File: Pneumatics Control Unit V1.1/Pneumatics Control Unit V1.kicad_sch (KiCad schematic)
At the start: 74 parts, among them J1 TX_PORT, J10 Conn_01x02_Male, J11 Conn_01x02_Male, J12 10118194-0001LF, J2 RX_PORT, J3 MICROMOD-2222, J4 Conn_01x02_Male, J5 Conn_01x02_Male, J6 Conn_01x02_Male, J7 Conn_01x02_Male, J8 Conn_01x02_Male, J9 Conn_01x02_Male, U1 ISL83490IBZ, U2 MIC2178-3.3YWM, U3 MC78M05CDTRKG, U4 MC78M05CDTRKG

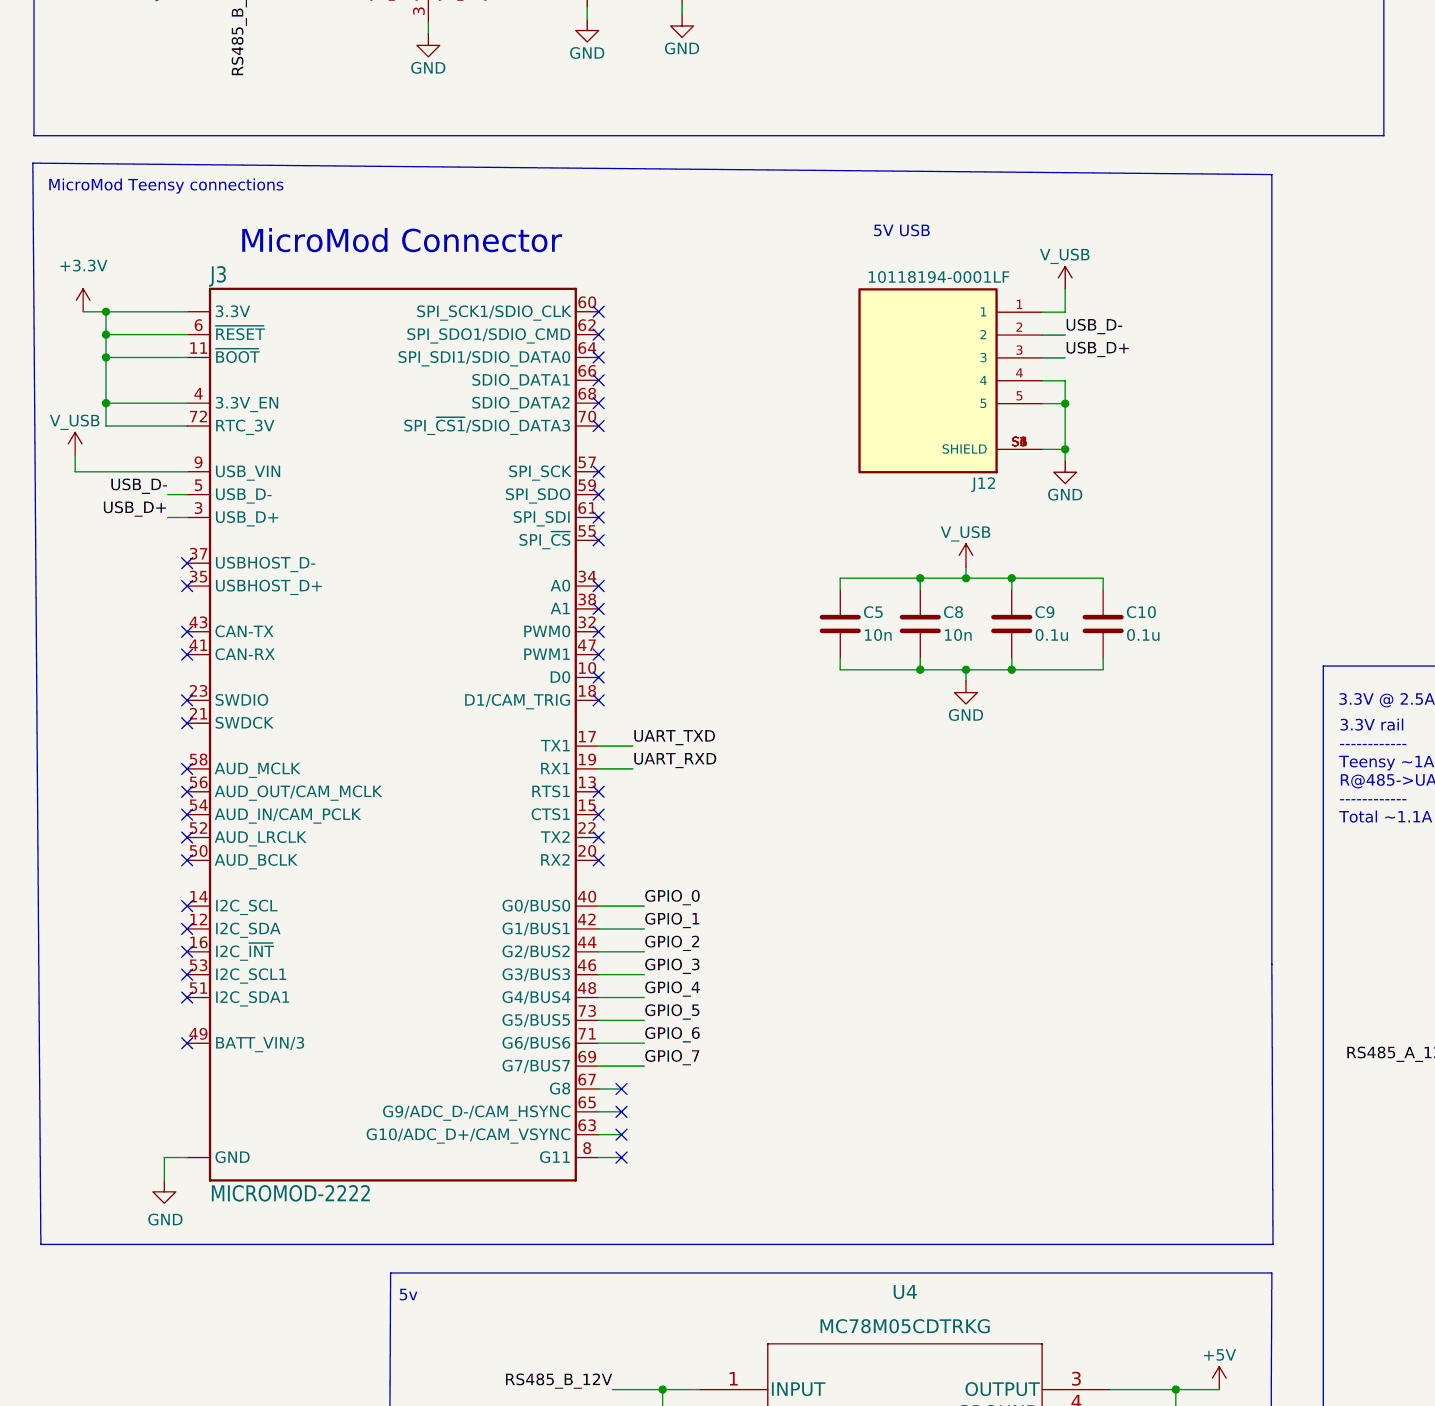
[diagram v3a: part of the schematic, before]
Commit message: Reducing vias, Thicken traces, adding resistors
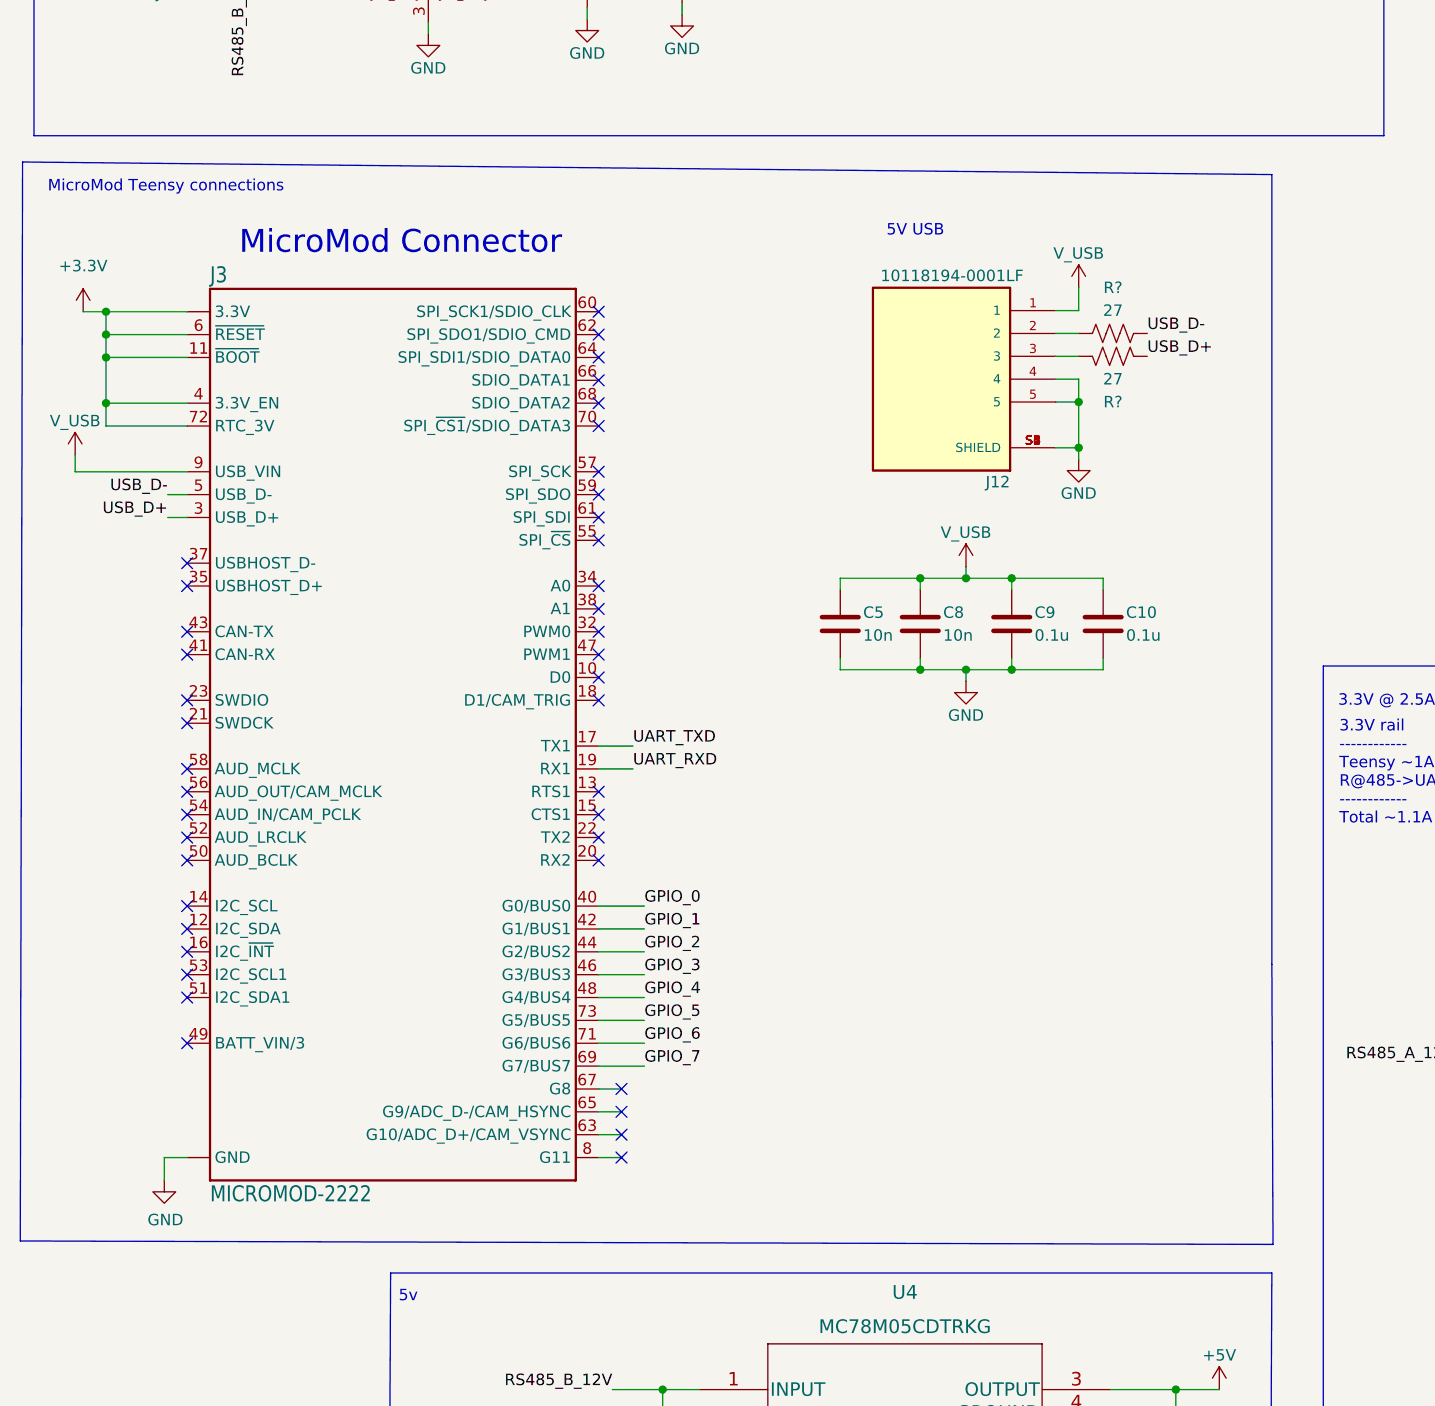
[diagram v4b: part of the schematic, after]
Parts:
- added R? (x2): 27, Resistor_SMD:R_0805_2012Metric_Pad1.20x1.40mm_HandSolder, symbol Device:R_US
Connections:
- net USB_D+: now also R?.2; no longer J12.3
- net USB_D-: now also R?.2; no longer J12.2
- new net: J12.2, R?.1
- new net: J12.3, R?.1
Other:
- moved on the sheet: J12

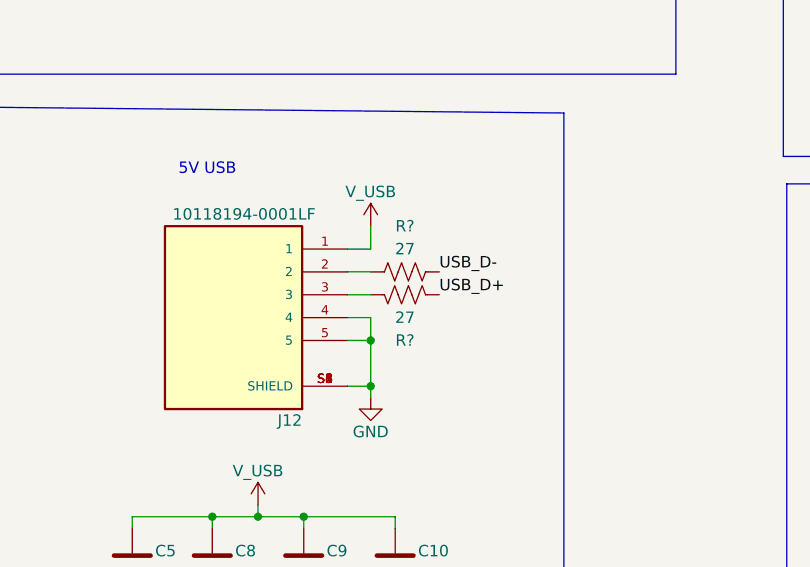
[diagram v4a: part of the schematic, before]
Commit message: Adding more grounding vias, and making the mouting holes 8-32
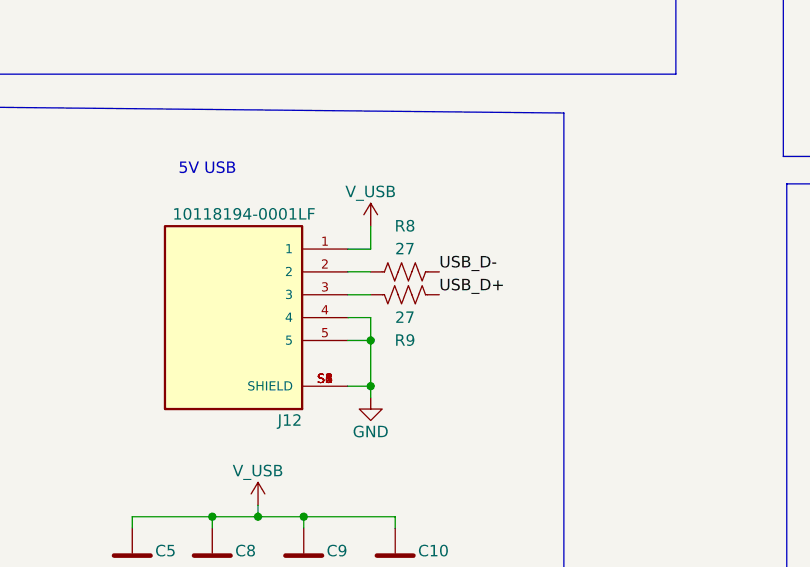
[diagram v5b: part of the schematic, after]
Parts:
- gave numbers to parts that had none: 2
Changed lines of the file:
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@@
   (symbol (lib_id "Device:R_US") (at 135.509 119.761 90) (unit 1)
     (in_bom yes) (on_board yes)
-    (property "Reference" "R?" (id 0) (at 135.509 114.681 90))
+    (property "Reference" "R8" (id 0) (at 135.509 114.681 90))
     (property "Value" "27" (id 1) (at 135.509 117.221 90))
     (property "Footprint" "Resistor_SMD:R_0805_2012Metric_Pad1.20x1.40mm_HandSolder" (id 2) (at 135.763 118.745 90)
@@
   (symbol (lib_id "Device:R_US") (at 135.509 122.301 90) (mirror x) (unit 1)
     (in_bom yes) (on_board yes)
-    (property "Reference" "R?" (id 0) (at 135.509 127.381 90))
+    (property "Reference" "R9" (id 0) (at 135.509 127.381 90))
     (property "Value" "27" (id 1) (at 135.509 124.841 90))
     (property "Footprint" "Resistor_SMD:R_0805_2012Metric_Pad1.20x1.40mm_HandSolder" (id 2) (at 135.763 123.317 90)
@@
     )
     (path "/f09ce1b1-fd65-4ae3-b44f-4ebb4de3bacb"
-      (reference "R?") (unit 1) (value "27") (footprint "Resistor_SMD:R_0805_2012Metric_Pad1.20x1.40mm_HandSolder")
+      (reference "R8") (unit 1) (value "27") (footprint "Resistor_SMD:R_0805_2012Metric_Pad1.20x1.40mm_HandSolder")
     )
     (path "/fcd7e2a1-c75c-4331-9afc-ca74c910ff4d"
-      (reference "R?") (unit 1) (value "27") (footprint "Resistor_SMD:R_0805_2012Metric_Pad1.20x1.40mm_HandSolder")
+      (reference "R9") (unit 1) (value "27") (footprint "Resistor_SMD:R_0805_2012Metric_Pad1.20x1.40mm_HandSolder")
     )
     (path "/097e0edc-0bee-47b5-b180-d68199aa4ff8"

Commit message: Adding 12V capabilities
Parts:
- added U (x2): (no value), symbol Connector:Conn_01x03_Male
- U: renamed from D6; value D_TVS_x2_AAC -> (none); footprint Package_TO_SOT_SMD:SOT-723 -> (none)
- U: renamed from C22; value 1u -> (none); footprint Capacitor_SMD:C_0805_2012Metric_Pad1.18x1.45mm_HandSolder -> (none)
- U: renamed from R7; value 10k -> (none); footprint Resistor_SMD:R_0805_2012Metric_Pad1.20x1.40mm_HandSolder -> (none)
- U: renamed from D10; value D_TVS_x2_AAC -> (none); footprint Package_TO_SOT_SMD:SOT-723 -> (none)
- U: renamed from H1; value MountingHole -> (none); footprint MountingHole:MountingHole_2.5mm -> (none)
- U: renamed from MOSFET5; value SSM3K7002KFU -> (none); footprint SSM3K7002KFU:SSM3K7002KFU -> (none)
- U: renamed from CR1; value MBRS130L -> (none); footprint MBRS130L:MBRS130L -> (none)
- U: renamed from C19; value 22uF -> (none); footprint 22U:CL21A226MQQNNNF -> (none)
- U: renamed from U1; value ISL83490IBZ -> (none); footprint RS_UART:ISL83490IBZ -> (none)
- U: renamed from MOSFET6; value SSM3K7002KFU -> (none); footprint SSM3K7002KFU:SSM3K7002KFU -> (none)
- U: renamed from C9; value 0.1u -> (none); footprint Capacitor_SMD:C_0805_2012Metric_Pad1.18x1.45mm_HandSolder -> (none)
- U: renamed from U4; value MC78M05CDTRKG -> (none); footprint 12v5v:MC78M05CDTRKG -> (none)
- U: renamed from MOSFET8; value SSM3K7002KFU -> (none); footprint SSM3K7002KFU:SSM3K7002KFU -> (none)
- U: renamed from J1; value TX_PORT -> (none); footprint RS485:RS485 -> (none)
- U: renamed from J12; value 10118194-0001LF -> (none); footprint 10118194-0001LF:AMPHENOL_10118194-0001LF -> (none)
- U: renamed from C5; value 10n -> (none); footprint Capacitor_SMD:C_0805_2012Metric_Pad1.18x1.45mm_HandSolder -> (none)
- U: renamed from J8; value Conn_01x02_Male -> (none); footprint Connector_PinSocket_2.54mm:PinSocket_1x02_P2.54mm_Vertical -> (none)
- U: renamed from U3; value MC78M05CDTRKG -> (none); footprint 12v5v:MC78M05CDTRKG -> (none)
- U: renamed from MOSFET3; value SSM3K7002KFU -> (none); footprint SSM3K7002KFU:SSM3K7002KFU -> (none)
- U: renamed from C17; value 22uF -> (none); footprint 22U:CL21A226MQQNNNF -> (none)
- U: renamed from C24; value 1u -> (none); footprint Capacitor_SMD:C_0805_2012Metric_Pad1.18x1.45mm_HandSolder -> (none)
- U: renamed from C18; value 22uF -> (none); footprint 22U:CL21A226MQQNNNF -> (none)
- U: renamed from J6; value Conn_01x02_Male -> (none); footprint Connector_PinSocket_2.54mm:PinSocket_1x02_P2.54mm_Vertical -> (none)
- U: renamed from C11; value CL21A226MQQNNNF (22uF) -> (none); footprint 22U:CL21A226MQQNNNF -> (none)
- U: renamed from C26; value 1u -> (none); footprint Capacitor_SMD:C_0805_2012Metric_Pad1.18x1.45mm_HandSolder -> (none)
- U: renamed from D9; value D_TVS_x2_AAC -> (none); footprint Package_TO_SOT_SMD:SOT-723 -> (none)
- U: renamed from L1; value LB3218T330M (33uH) -> (none); footprint induct33u:LB3218T330M -> (none)
- U: renamed from C6; value 6.8n -> (none); footprint Capacitor_SMD:C_0805_2012Metric_Pad1.18x1.45mm_HandSolder -> (none)
- U: renamed from C12; value 22uF -> (none); footprint 22U:CL21A226MQQNNNF -> (none)
- U: renamed from J9; value Conn_01x02_Male -> (none); footprint Connector_PinSocket_2.54mm:PinSocket_1x02_P2.54mm_Vertical -> (none)
- U: renamed from D1; value D_TVS_x2_AAC -> (none); footprint Package_TO_SOT_SMD:SOT-723 -> (none)
- U: renamed from R6; value 10k -> (none); footprint Resistor_SMD:R_0805_2012Metric_Pad1.20x1.40mm_HandSolder -> (none)
- U: renamed from C10; value 0.1u -> (none); footprint Capacitor_SMD:C_0805_2012Metric_Pad1.18x1.45mm_HandSolder -> (none)
- U: renamed from C15; value 22uF -> (none); footprint 22U:CL21A226MQQNNNF -> (none)
- U: renamed from H3; value MountingHole -> (none); footprint MountingHole:MountingHole_2.5mm -> (none)
- U: renamed from MOSFET2; value SSM3K7002KFU -> (none); footprint SSM3K7002KFU:SSM3K7002KFU -> (none)
- U: renamed from J4; value Conn_01x02_Male -> (none); footprint Connector_PinSocket_2.54mm:PinSocket_1x02_P2.54mm_Vertical -> (none)
- U: renamed from J5; value Conn_01x02_Male -> (none); footprint Connector_PinSocket_2.54mm:PinSocket_1x02_P2.54mm_Vertical -> (none)
- U: renamed from D2; value D_TVS_x2_AAC -> (none); footprint Package_TO_SOT_SMD:SOT-723 -> (none)
- U: renamed from J3; value MICROMOD-2222 -> (none); footprint mm-m:M.2-CONNECTOR-E -> (none)
- U: renamed from D3; value D_TVS_x2_AAC -> (none); footprint Package_TO_SOT_SMD:SOT-723 -> (none)
- U: renamed from U2; value MIC2178-3.3YWM -> (none); footprint 33sw:MIC2178-3.3YWM -> (none)
- U: renamed from C21; value 22uF -> (none); footprint 22U:CL21A226MQQNNNF -> (none)
- U: renamed from R2; value 10 -> (none); footprint Resistor_SMD:R_0805_2012Metric_Pad1.20x1.40mm_HandSolder -> (none)
- U: renamed from MOSFET1; value SSM3K7002KFU -> (none); footprint SSM3K7002KFU:SSM3K7002KFU -> (none)
- U: renamed from C23; value 1u -> (none); footprint Capacitor_SMD:C_0805_2012Metric_Pad1.18x1.45mm_HandSolder -> (none)
- U: renamed from J10; value Conn_01x02_Male -> (none); footprint Connector_PinSocket_2.54mm:PinSocket_1x02_P2.54mm_Vertical -> (none)
- U: renamed from D7; value D_TVS_x2_AAC -> (none); footprint Package_TO_SOT_SMD:SOT-723 -> (none)
- U: renamed from C27; value 0.1u -> (none); footprint Capacitor_SMD:C_0805_2012Metric_Pad1.18x1.45mm_HandSolder -> (none)
- U: renamed from C14; value 22uF -> (none); footprint 22U:CL21A226MQQNNNF -> (none)
- U: renamed from H2; value MountingHole -> (none); footprint MountingHole:MountingHole_2.5mm -> (none)
- U: renamed from MOSFET7; value SSM3K7002KFU -> (none); footprint SSM3K7002KFU:SSM3K7002KFU -> (none)
- U: renamed from C25; value 1u -> (none); footprint Capacitor_SMD:C_0805_2012Metric_Pad1.18x1.45mm_HandSolder -> (none)
- U: renamed from R4; value 10 -> (none); footprint Resistor_SMD:R_0805_2012Metric_Pad1.20x1.40mm_HandSolder -> (none)
- U: renamed from C1; value 0.1u -> (none); footprint Capacitor_SMD:C_0805_2012Metric_Pad1.18x1.45mm_HandSolder -> (none)
- U: renamed from C13; value 22uF -> (none); footprint 22U:CL21A226MQQNNNF -> (none)
- U: renamed from D8; value D_TVS_x2_AAC -> (none); footprint Package_TO_SOT_SMD:SOT-723 -> (none)
- U: renamed from J7; value Conn_01x02_Male -> (none); footprint Connector_PinSocket_2.54mm:PinSocket_1x02_P2.54mm_Vertical -> (none)
- U: renamed from C16; value 22uF -> (none); footprint 22U:CL21A226MQQNNNF -> (none)
- U: renamed from C7; value 0.01u -> (none); footprint Capacitor_SMD:C_0805_2012Metric_Pad1.18x1.45mm_HandSolder -> (none)
- U: renamed from C20; value 22uF -> (none); footprint 22U:CL21A226MQQNNNF -> (none)
- U: renamed from MOSFET4; value SSM3K7002KFU -> (none); footprint SSM3K7002KFU:SSM3K7002KFU -> (none)
- U: renamed from J11; value Conn_01x02_Male -> (none); footprint Connector_PinSocket_2.54mm:PinSocket_1x02_P2.54mm_Vertical -> (none)
- U: renamed from D4; value D_TVS_x2_AAC -> (none); footprint Package_TO_SOT_SMD:SOT-723 -> (none)
- U: renamed from C2; value 0.1u -> (none); footprint Capacitor_SMD:C_0805_2012Metric_Pad1.18x1.45mm_HandSolder -> (none)
- U: renamed from C4; value 0.1u -> (none); footprint Capacitor_SMD:C_0805_2012Metric_Pad1.18x1.45mm_HandSolder -> (none)
- U: renamed from R5; value 20k -> (none); footprint Resistor_SMD:R_0805_2012Metric_Pad1.20x1.40mm_HandSolder -> (none)
- U: renamed from C8; value 10n -> (none); footprint Capacitor_SMD:C_0805_2012Metric_Pad1.18x1.45mm_HandSolder -> (none)
- U: renamed from R8; value 27 -> (none); footprint Resistor_SMD:R_0805_2012Metric_Pad1.20x1.40mm_HandSolder -> (none)
- U: renamed from R3; value 10 -> (none); footprint Resistor_SMD:R_0805_2012Metric_Pad1.20x1.40mm_HandSolder -> (none)
- U: renamed from J2; value RX_PORT -> (none); footprint RS485:RS485 -> (none)
- U: renamed from R1; value 10 -> (none); footprint Resistor_SMD:R_0805_2012Metric_Pad1.20x1.40mm_HandSolder -> (none)
- U: renamed from H4; value MountingHole -> (none); footprint MountingHole:MountingHole_2.5mm -> (none)
- U: renamed from D5; value D_TVS_x2_AAC -> (none); footprint Package_TO_SOT_SMD:SOT-723 -> (none)
- U: renamed from C3; value 0.1u -> (none); footprint Capacitor_SMD:C_0805_2012Metric_Pad1.18x1.45mm_HandSolder -> (none)
- U: renamed from R9; value 27 -> (none); footprint Resistor_SMD:R_0805_2012Metric_Pad1.20x1.40mm_HandSolder -> (none)
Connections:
- net RS485_B_12V: now also U.3 (Pin_3), U.3 (Pin_3)
- net solenoid_power: now reaches U.2 (Pin_2)
- net solenoid_power: now also U.2 (Pin_2), U.2 (Pin_2), U.2 (Pin_2), U.2 (Pin_2)
- net solenoid_power_2: now reaches U.2 (Pin_2)
- net solenoid_power_2: now also U.2 (Pin_2), U.2 (Pin_2), U.2 (Pin_2), U.2 (Pin_2)
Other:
- moved on the sheet: U

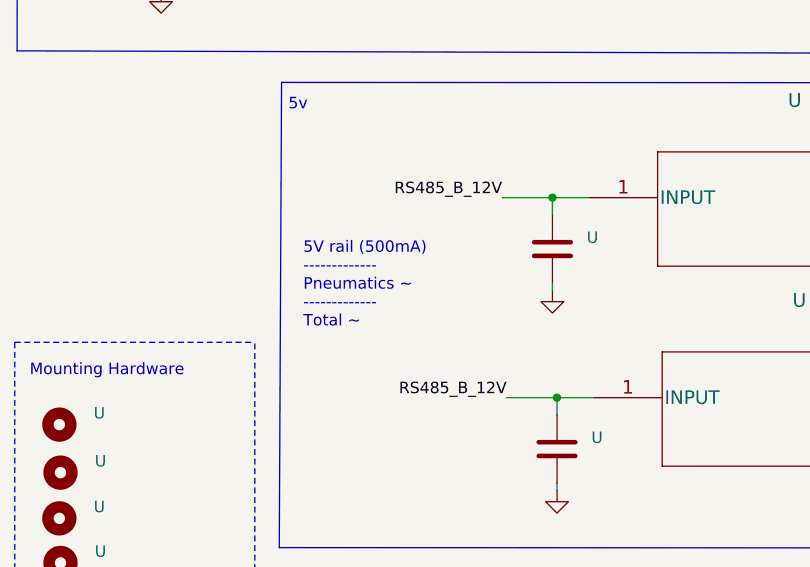
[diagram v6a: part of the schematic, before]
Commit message: Adding current draw on 5v rail
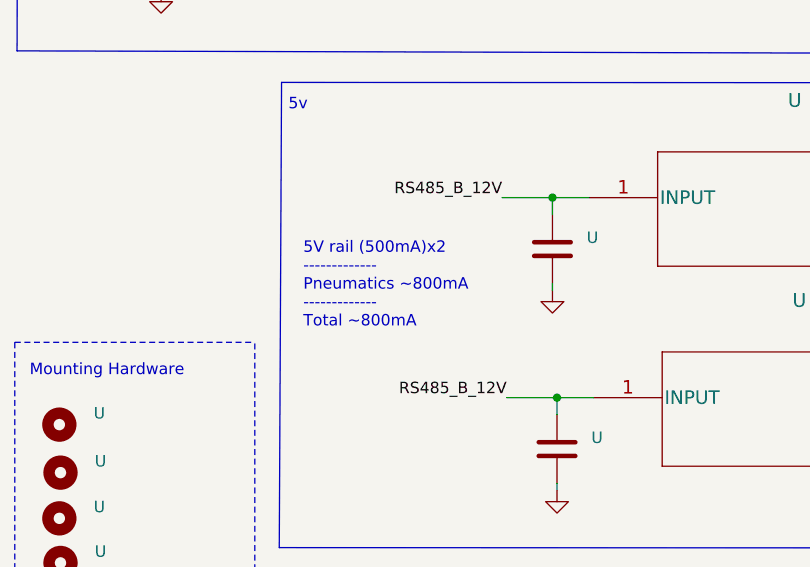
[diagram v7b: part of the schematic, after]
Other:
- note added: "5V rail (500mA)x2 ------------- Pneumatics ~800mA ------------- Total ~800mA"
- note removed: "5V rail (500mA) ------------- Pneumatics ~ ------------- Total ~"
